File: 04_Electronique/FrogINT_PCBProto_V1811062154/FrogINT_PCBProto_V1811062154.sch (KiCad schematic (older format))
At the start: 32 parts, among them J1 USB_B_Mini, J2 Conn_01x01_Female, J3 Conn_01x03, J4 JTAG, Q1 PMV48XP, Q2 PMV48XP, U1 NCP1117-5.0_SOT223, U2 LP2985-3.3, U3 ATmega16U4RC-AU, Y1 16MHz

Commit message: Commit du 26/03/2019 :
 - Refonte du PCB --> passage en circulaire de 3,8mm de diamètre
 - Mise à jour des librairies avec notamment création de la librairie atmega16u4-au
 - Mise à jour de la librairie sur le connecteur USB pour ajouter les CTRL.YBCK -> limite du composant
 - Suppression de la fonction d'alimention 3V3 au profit d'une seule alimentation en 5V. Attention, il faut cependant corriger le naming
 - Changement du connecteur pour le TouchSensor (femelle)
 - ajout d'un R/C + pad pour souder directement une antenne pour tester le Sensor Capacitif
 - suppression du bouton reset et du bouton interrupt.
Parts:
- removed C10, C3: 100nF, FTA_FrogINT_Library_Footprint_Package:CP_EIA-2012-12_Kemet-R, symbol Device:C
- removed C4, C7: 0.1µF, FTA_FrogINT_Library_Footprint_Package:CP_EIA-2012-12_Kemet-R, symbol Device:C
- removed C8: 1µF, FTA_FrogINT_Library_Footprint_Package:CP_EIA-2012-12_Kemet-R, symbol Device:C
- removed C9: 22µF, FTA_FrogINT_Library_Footprint_Package:CP_EIA-2012-12_Kemet-R, symbol Device:CP
- removed J2: Conn_01x01_Female, TestPoint:TestPoint_Pad_D1.0mm, symbol Connector:Conn_01x01_Female
- removed Q1, Q2: PMV48XP, Package_TO_SOT_SMD:SOT-23-6, symbol Device:Q_PMOS_DGS
- removed R4: 10k, FTA_FrogINT_Library_Footprint_Package:R_0603_1608Metric, symbol Device:R
- removed S1: PTS810SJG250SMTRLFS, SamacSys_Parts:PTS810SJG250SMTRLFS, symbol FrogINT_PCBProto_V1811062154-rescue:PTS810SJG250SMTRLFS-SamacSys_Parts
- removed U1: NCP1117-5.0_SOT223, Package_TO_SOT_SMD:SOT-223-3_TabPin2, symbol Regulator_Linear:NCP1117-5.0_SOT223
- removed U2: LP2985-3.3, Package_TO_SOT_SMD:SOT-23-5, symbol Regulator_Linear:LP2985-3.3
- removed U3: ATmega16U4RC-AU, FTA_FrogINT_Library_Footprint_Package:TQFP-44_10x10mm_P0.8mm, symbol FrogINT_PCBProto_V1811062154-cache:ATmega16U4RC-AU
- added C11: 22pF, FTA_FrogINT_Library_Footprint_Package:CP_EIA-2012-12_Kemet-R, symbol Device:C
- added J5: Conn_01x01_Female, TestPoint:TestPoint_THTPad_D2.5mm_Drill1.2mm, symbol Connector:Conn_01x01_Female
- added U3: ATmega16U4-AU, Package_QFP:TQFP-44_10x10mm_P0.8mm, symbol atmega16u4-au:ATmega16U4-AU
- J3: footprint Connector_PinHeader_2.54mm:PinHeader_1x03_P2.54mm_Horizontal -> Connector_PinSocket_2.54mm:PinSocket_1x03_P2.54mm_Horizontal
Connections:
- net labels removed: +5V, VBUS, Vin
- wire segments 157 -> 111
- no-connect marks 22 -> 21
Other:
- note added: "Body / Finger to touch"

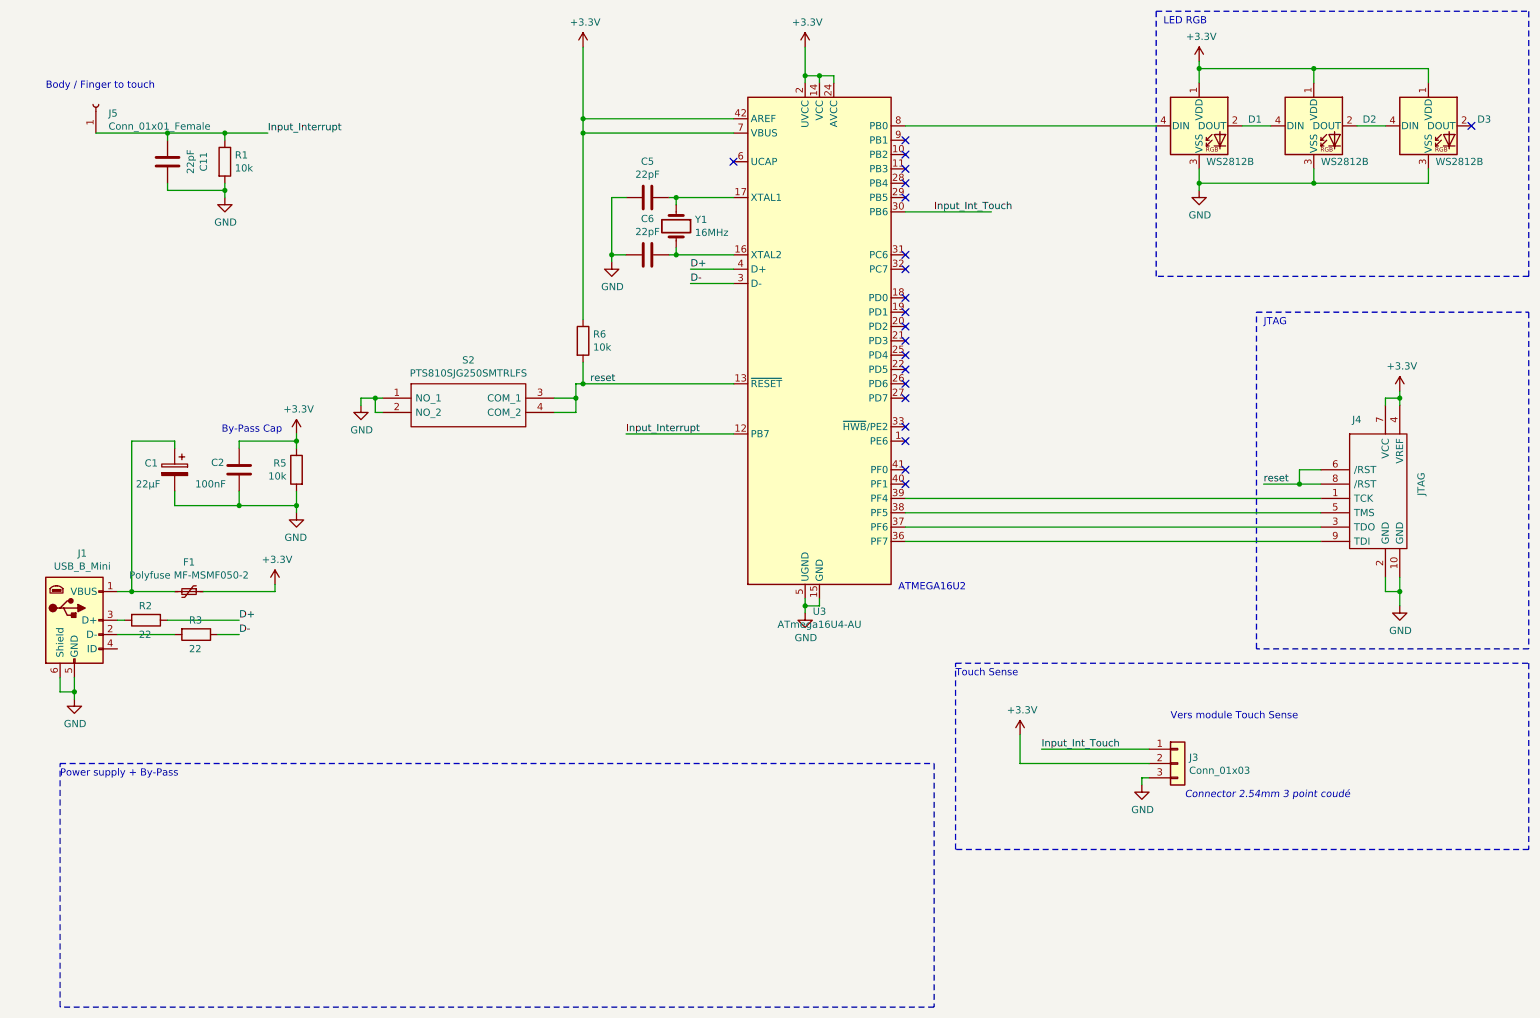
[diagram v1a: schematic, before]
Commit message: Evolution de la V3 :
 + Creation d'un modèle pour les LED WS2812 avec HeatSink (Footprint + meca3D)
 + Creation d'un modèle pour Fusible (Footprint + Meca3D)

Autre évolution majeure :
•	Ligne USB – Faire une paire différentielle
•	Supprimer le switch « normal » pour ne conserver que le switch « reset ».
o	OK
•	Mais router en externe une GPIO
o	OK mutualisé avec R/C pour Touche sensor
•	Suppression du TouchPad au profit d’un connecteur 2.54 coudé – femelle. ATTENTION actuellement de type mâle à remplacer à femelle.
o	OK
o	Genre du header à remplacer de mâle à femelle
•	Ajouter R & C pour tester le TouchPanel avec une feuille d’alu.
o	OK mutualisé avec R/C pour Touche sensor
•	Créer une Pin externe avec de connecter la feuille d’alu.
o	OK mutualisé avec R/C pour Touche sensor
•	Supprimer la génération du 5V non nécessaire
o	Laisser en l’état
•	Supprimer la pin de mesure de 5V
o	Laisser en l’état
•	Remplacement connecteur JTAG au pas de 2.54 par un au pas de 1,27 qui doit rester compatible avec interface ATMEL-Ice.
o	OK en cours.
o	Pinout à vérifier.
•	Remplacement du Quartz par un modèle 3.2x2.4
o	OK
•	Mise à jour du modèle 3D du fusible
o	OK
•	routage dont ligne différentielle.
o	OK
•	Passer à diamètre supérieur le PCB
o	OK
•	Remplacer le package des LED
o	OK
•	Mise à jour de la BOM RadioSpare
o	OK
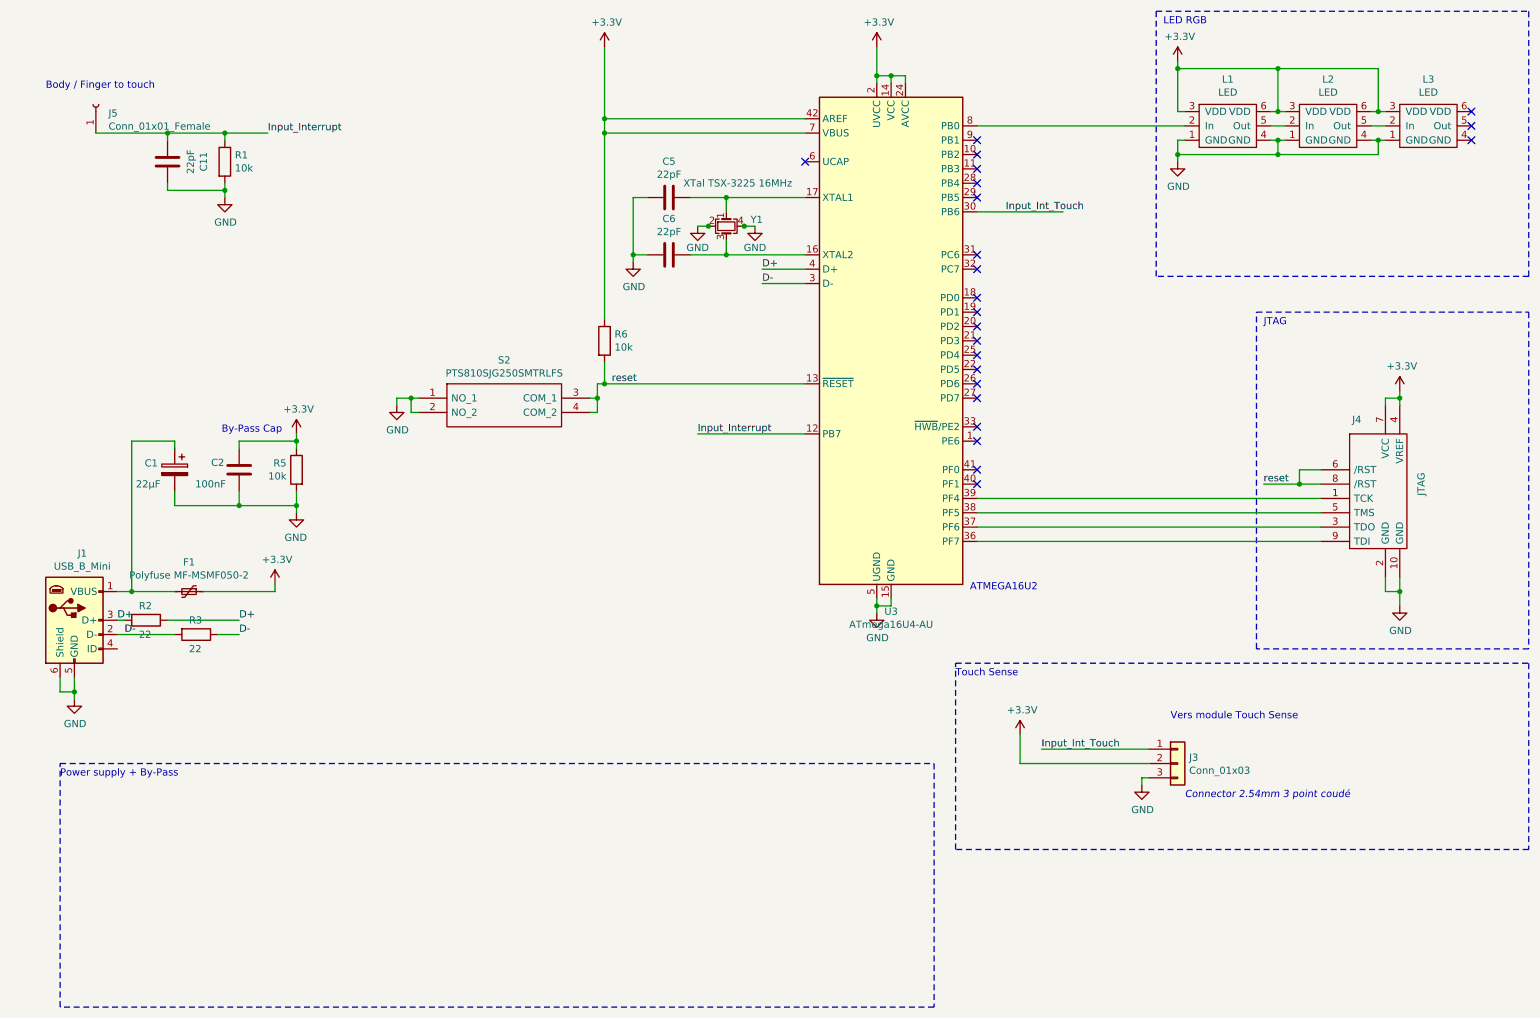
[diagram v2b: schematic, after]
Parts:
- removed D1, D2, D3: WS2812B, FTA_FrogINT_Library_Footprint_Package:LED_WS2812B_PLCC4_5.0x5.0mm_P3.2mm, symbol LED:WS2812B
- removed Y1: 16MHz, FTA_FrogINT_Library_Footprint_Package:Crystal_HC49-U_Vertical, symbol Device:Crystal
- added L1, L2, L3: LED, FTA_FrogINT_Library_Footprint_Package:WS2812-LED_HeatSink, symbol FTA_FrogINT_library:LED
- added Y1: XTal TSX-3225 16MHz, Crystal:Crystal_SMD_SeikoEpson_TSX3225-4Pin_3.2x2.5mm_HandSoldering, symbol Device:Crystal_GND24_Small
- F1: footprint Fuse:Fuse_1206_3216Metric -> FTA_FrogINT_Library_Footprint_Package:FUSC4632X85N
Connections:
- net +3V3: now also L1.3 (VDD), L1.6 (VDD), L2.3 (VDD), L2.6 (VDD), L3.3 (VDD)
- net D+: now also J1.3 (D+), R2.2
- net D-: now also J1.2 (D-), R3.2
- net GND: now also L1.1 (GND), L1.4 (GND), L2.1 (GND), L2.4 (GND), L3.1 (GND), Y1.2, Y1.4
- net at U3.8 (PB0): now also L1.2 (In)
- net at C5.1, U3.17 (XTAL1): now also Y1.1
- net at C6.1, U3.16 (XTAL2): now also Y1.3
- new net: L1.5 (Out), L2.2 (In)
- new net: L2.5 (Out), L3.2 (In)
- no-connect marks 21 -> 23
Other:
- moved on the sheet: C5, C6, R6, S2, U3
